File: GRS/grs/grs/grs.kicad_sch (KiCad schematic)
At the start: 4 parts, among them U1 Teensy4.1, U2 TSR1-2450E, U3 BME280

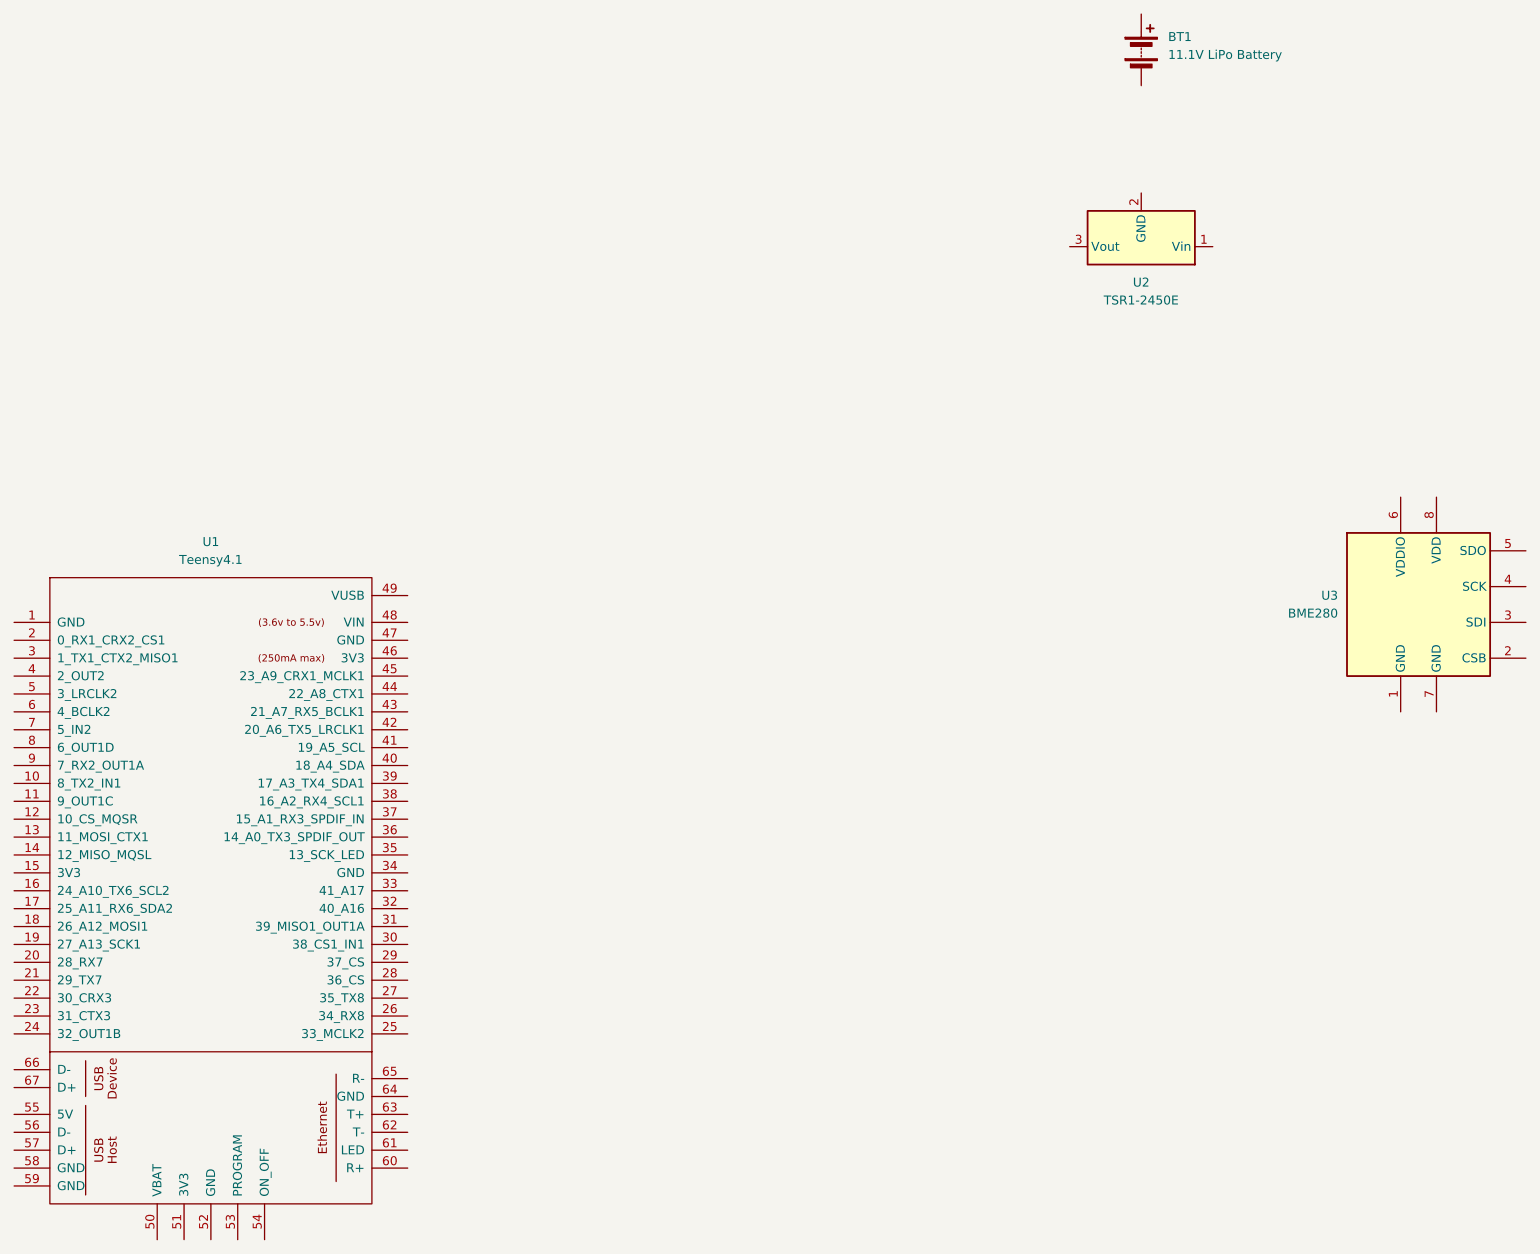
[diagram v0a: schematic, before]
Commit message: added valve symb and wires
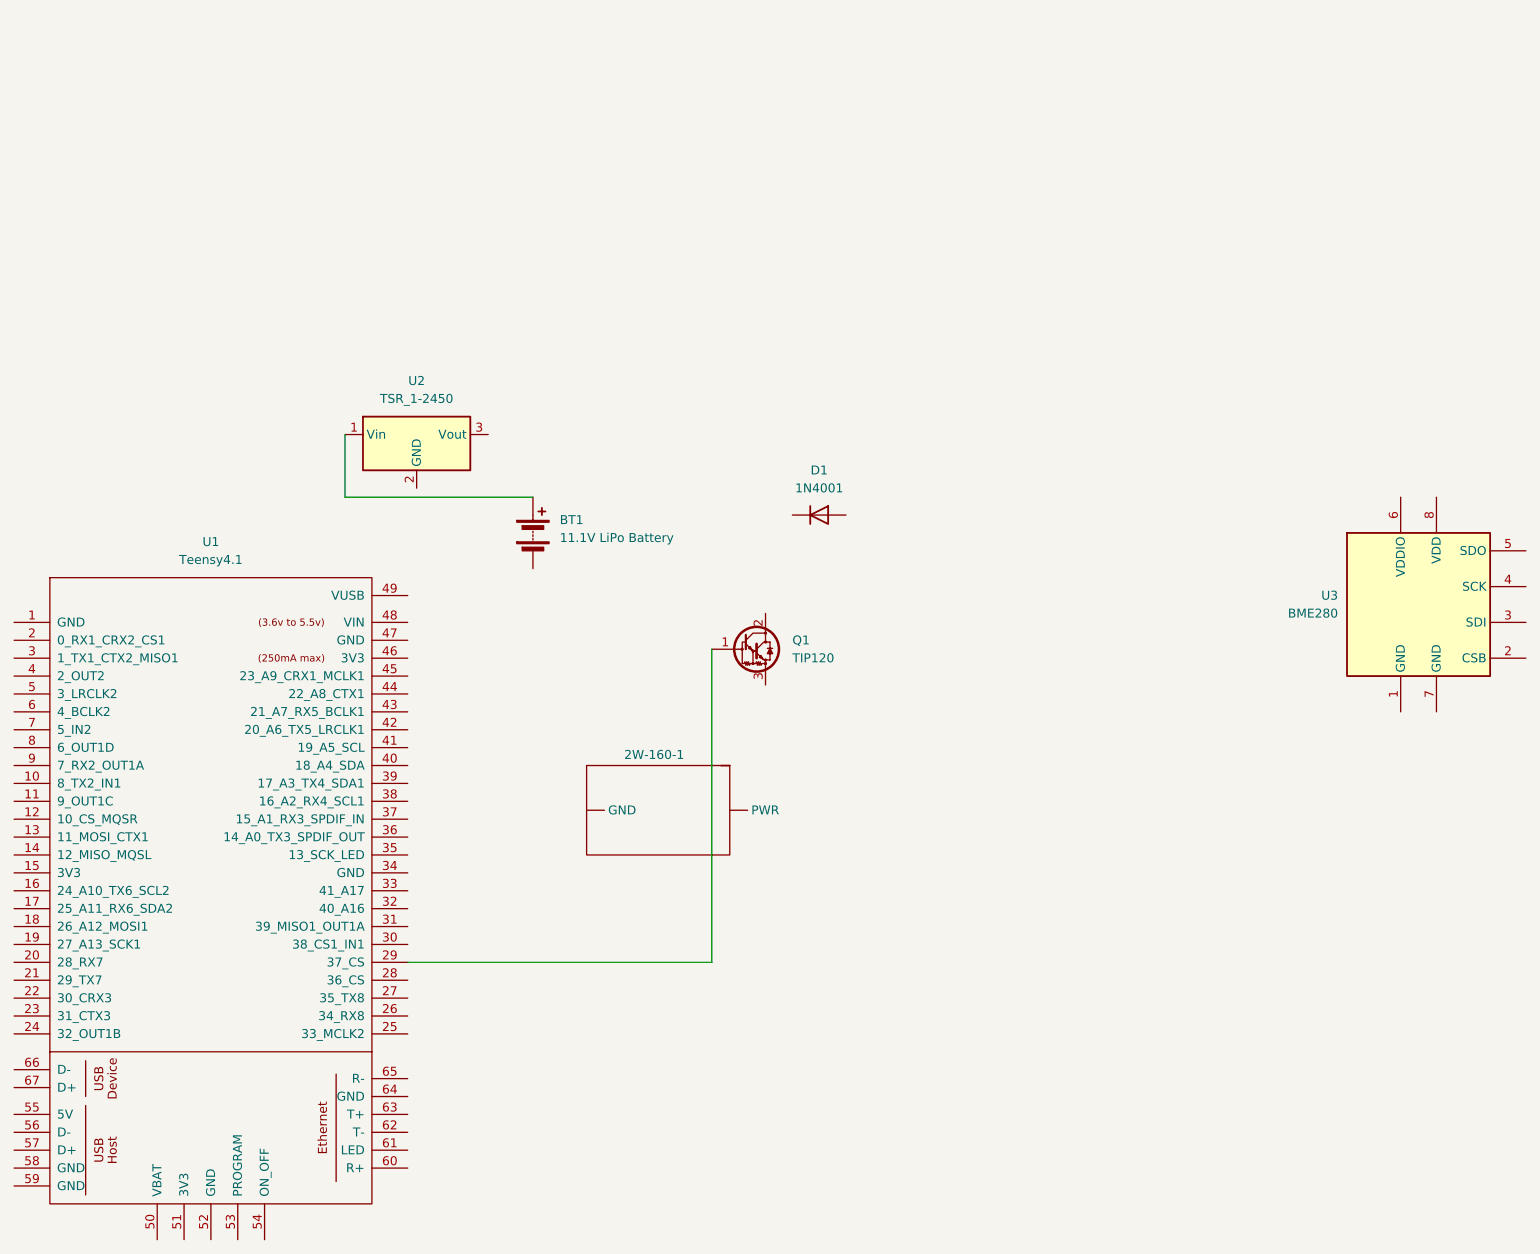
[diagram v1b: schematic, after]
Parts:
- removed U2: TSR1-2450E, Converter_DCDC:Converter_DCDC_TRACO_TSR1-xxxxE_THT, symbol Regulator_Switching:TSR1-2450E
- added 2W-160-1: ~, symbol GRS_Valve:2W-160-15
- added D1: 1N4001, Diode_THT:D_DO-41_SOD81_P10.16mm_Horizontal, symbol Diode:1N4001
- added Q1: TIP120, Package_TO_SOT_THT:TO-220-3_Vertical, symbol Transistor_BJT:TIP120
- added U2: TSR_1-2450, Converter_DCDC:Converter_DCDC_TRACO_TSR-1_THT, symbol Regulator_Switching:TSR_1-2450
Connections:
- net at U1.29 (37_CS): now also Q1.1 (B)
- net at BT1.1 (+): now also U2.1 (Vin)
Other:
- moved on the sheet: BT1
